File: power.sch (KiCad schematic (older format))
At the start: 19 parts, among them P1 CONN_01X02, P2 CONN_01X02, P3 CONN_01X02, P4 CONN_01X02, U1 MC34063

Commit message: - added wifi esp8266 - switched caps to smd - fixed dual transistor pinout bug
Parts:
- C1, C2: footprint capacitors:C_0805 -> capacitors:C_1206
- U1: symbol MC34063 -> MC34063-RESCUE-rados
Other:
- moved on the sheet: R1, R2, R3
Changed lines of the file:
@@
 EESchema Schematic File Version 2
+LIBS:rados-rescue
+LIBS:import-transistors
+LIBS:import-regulators
+LIBS:import-opamps
+LIBS:import-diodes
 LIBS:led_reverse
 LIBS:arduino_shieldsNCL
 LIBS:otheruse_transistors
 LIBS:custom_power
-LIBS:import_resistors
-LIBS:import_regulators
-LIBS:import_transistors
-LIBS:import_diodes
+LIBS:import-misc
+LIBS:armin_misc
 LIBS:power
 LIBS:device
 LIBS:transistors
 LIBS:conn
-LIBS:import_misc
 LIBS:linear
 LIBS:regul
@@
 LIBS:valves
 LIBS:arduino
+LIBS:ESP8266
 LIBS:rados-cache
 EELAYER 25 0
@@
 	4400 1925 4400 2625
 $Comp
-L MC34063 U1
+L MC34063-RESCUE-rados U1
 U 1 1 568AB185
 P 2025 2100
+AR Path="/568AB185" Ref="U1"  Part="1"
+AR Path="/568AA436/568AB185" Ref="U1"  Part="1"
 F 0 "U1" H 2425 2475 34  0000 C BNN
 F 1 "MC34063" H 2425 2150 34  0000 C BNN
@@
 $EndComp
 Wire Wire Line
-	1525 1925 2075 1925
+	1525 1925 2025 1925
 $Comp
 L STPS3L40UF D1
@@
 L RESISTOR R2
 U 1 1 568AB18A
-P 3725 1825
-F 0 "R2" V 3875 1750 34  0000 L BNN
-F 1 "10K" H 3825 1900 34  0000 L BNN
-F 2 "resistors:R_0603" H 3725 1825 60  0001 C CNN
-F 3 "" H 3725 1825 60  0000 C CNN
-	1    3725 1825
+P 3675 1825
+F 0 "R2" V 3825 1750 34  0000 L BNN
+F 1 "10K" H 3775 1900 34  0000 L BNN
+F 2 "resistors:R_0603" H 3675 1825 60  0001 C CNN
+F 3 "" H 3675 1825 60  0000 C CNN
+	1    3675 1825
 	0    1    1    0
 $EndComp
@@
 L RESISTOR R3
 U 1 1 568AB18B
-P 3725 2100
-F 0 "R3" V 3875 2175 34  0000 L BNN
-F 1 "1K1" H 3800 2050 34  0000 L BNN
-F 2 "resistors:R_0603" H 3725 2100 60  0001 C CNN
-F 3 "" H 3725 2100 60  0000 C CNN
-	1    3725 2100
+P 3675 2100
+F 0 "R3" V 3825 2175 34  0000 L BNN
+F 1 "1K1" H 3750 2050 34  0000 L BNN
+F 2 "resistors:R_0603" H 3675 2100 60  0001 C CNN
+F 3 "" H 3675 2100 60  0000 C CNN
+	1    3675 2100
 	0    1    1    0
 $EndComp
@@
 L RESISTOR R1
 U 1 1 568AB18D
-P 1750 1850
-F 0 "R1" H 1850 1900 34  0000 L BNN
-F 1 "0.22R" H 1800 1800 34  0000 L BNN
-F 2 "resistors:R_1206" H 1750 1850 60  0001 C CNN
-F 3 "" H 1750 1850 60  0000 C CNN
-	1    1750 1850
+P 1750 1900
+F 0 "R1" H 1825 2025 34  0000 L BNN
+F 1 "0.22R" H 1800 1900 34  0000 L BNN
+F 2 "resistors:R_1206" H 1750 1900 60  0001 C CNN
+F 3 "" H 1750 1900 60  0000 C CNN
+	1    1750 1900
 	1    0    0    -1
 $EndComp
@@
 F 0 "C1" H 1535 2145 50  0000 L CNN
 F 1 "10uF" H 1535 1995 50  0000 L CNN
-F 2 "capacitors:C_0805" H 1525 2075 50  0001 C CNN
+F 2 "capacitors:C_1206" H 1525 2075 50  0001 C CNN
 F 3 "" H 1525 2075 50  0000 C CNN
 	1    1525 2075
@@
 F 0 "C2" H 1760 2145 50  0000 L CNN
 F 1 "10uF" H 1760 1995 50  0000 L CNN
-F 2 "capacitors:C_0805" H 1750 2075 50  0001 C CNN
+F 2 "capacitors:C_1206" H 1750 2075 50  0001 C CNN
 F 3 "" H 1750 2075 50  0000 C CNN
 	1    1750 2075
@@
 $EndComp
 $Comp
-L +12V #PWR06
+L +12V #PWR49
 U 1 1 568AC408
 P 5150 1925
-F 0 "#PWR06" H 5150 1775 50  0001 C CNN
+F 0 "#PWR49" H 5150 1775 50  0001 C CNN
 F 1 "+12V" H 5168 2099 50  0000 C CNN
 F 2 "" H 5150 1925 50  0000 C CNN
@@
 $EndComp
 $Comp
-L GND #PWR07
+L GND #PWR4
 U 1 1 568AE875
 P 1425 4450
-F 0 "#PWR07" H 1425 4200 50  0001 C CNN
+F 0 "#PWR4" H 1425 4200 50  0001 C CNN
 F 1 "GND" H 1433 4276 50  0000 C CNN
 F 2 "" H 1425 4450 50  0000 C CNN
@@
 $EndComp
 $Comp
-L GND #PWR08
+L GND #PWR23
 U 1 1 568AE8A5
 P 2800 2325
-F 0 "#PWR08" H 2800 2075 50  0001 C CNN
+F 0 "#PWR23" H 2800 2075 50  0001 C CNN
 F 1 "GND" H 2808 2151 50  0000 C CNN
 F 2 "" H 2800 2325 50  0000 C CNN
@@
 	1500 4350 1425 4350
 $Comp
-L Vsupply #P09
+L Vsupply #P11
 U 1 1 568AD53F
 P 4750 1225
-F 0 "#P09" H 4750 1225 60  0001 C CNN
+F 0 "#P11" H 4750 1225 60  0001 C CNN
 F 1 "Vsupply" H 4750 1175 34  0000 C CNN
 F 2 "" H 4750 1225 60  0000 C CNN
@@
 $EndComp
 $Comp
-L Vsupply #P010
+L Vsupply #P1
 U 1 1 568AD70E
 P 1525 1775
-F 0 "#P010" H 1525 1775 60  0001 C CNN
+F 0 "#P1" H 1525 1775 60  0001 C CNN
 F 1 "Vsupply" H 1525 1725 34  0000 C CNN
 F 2 "" H 1525 1775 60  0000 C CNN
@@
 $EndComp
 $Comp
-L GND #PWR011
+L GND #PWR6
 U 1 1 568ADBA9
 P 1450 3800
-F 0 "#PWR011" H 1450 3550 50  0001 C CNN
+F 0 "#PWR6" H 1450 3550 50  0001 C CNN
 F 1 "GND" H 1458 3626 50  0000 C CNN
 F 2 "" H 1450 3800 50  0000 C CNN
@@
 	1525 3700 1450 3700
 $Comp
-L Vsupply #P012
+L Vsupply #P4
 U 1 1 568ADC9C
 P 2125 3550
-F 0 "#P012" H 2125 3550 60  0001 C CNN
+F 0 "#P4" H 2125 3550 60  0001 C CNN
 F 1 "Vsupply" H 2125 3500 34  0000 C CNN
 F 2 "" H 2125 3550 60  0000 C CNN
@@
 $EndComp
 $Comp
-L Vheatbed #P013
+L Vheatbed #P3
 U 1 1 568AE31D
 P 2100 4200
-F 0 "#P013" H 2100 4200 60  0001 C CNN
+F 0 "#P3" H 2100 4200 60  0001 C CNN
 F 1 "Vheatbed" H 2100 4150 34  0000 C CNN
 F 2 "" H 2100 4200 60  0000 C CNN
@@
 $EndComp
 $Comp
-L GND #PWR014
+L GND #PWR9
 U 1 1 568AE68D
 P 1475 5400
-F 0 "#PWR014" H 1475 5150 50  0001 C CNN
+F 0 "#PWR9" H 1475 5150 50  0001 C CNN
 F 1 "GND" H 1483 5226 50  0000 C CNN
 F 2 "" H 1475 5400 50  0000 C CNN
@@
 	1475 5300 1650 5300
 $Comp
-L Vsupply #P015
+L Vsupply #P2
 U 1 1 568AE69B
 P 1650 5150
-F 0 "#P015" H 1650 5150 60  0001 C CNN
+F 0 "#P2" H 1650 5150 60  0001 C CNN
 F 1 "Vsupply" H 1650 5100 34  0000 C CNN
 F 2 "" H 1650 5150 60  0000 C CNN
@@
 $EndComp
 $Comp
-L GND #PWR016
+L GND #PWR10
 U 1 1 568AE860
 P 1475 6475
-F 0 "#PWR016" H 1475 6225 50  0001 C CNN
+F 0 "#PWR10" H 1475 6225 50  0001 C CNN
 F 1 "GND" H 1483 6301 50  0000 C CNN
 F 2 "" H 1475 6475 50  0000 C CNN
@@
 	1475 6375 1650 6375
 $Comp
-L +12V #PWR017
+L +12V #PWR11
 U 1 1 568BD457
 P 1650 6375
-F 0 "#PWR017" H 1650 6225 50  0001 C CNN
+F 0 "#PWR11" H 1650 6225 50  0001 C CNN
 F 1 "+12V" H 1668 6549 50  0000 C CNN
 F 2 "" H 1650 6375 50  0000 C CNN

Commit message: Routing
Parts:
- added P23, P24: CONN_01X02, headers:CON_HDR_1x2_2.54mm, symbol CONN_01X02
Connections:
- net +12V: now also P24.2 (P2)
- net GND: now also P23.1 (P1), P24.1 (P1)
- net Vsupply: now also P23.2 (P2)
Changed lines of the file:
@@
 $EndComp
 $Comp
-L +12V #PWR49
+L +12V #PWR15
 U 1 1 568AC408
 P 5150 1925
-F 0 "#PWR49" H 5150 1775 50  0001 C CNN
+F 0 "#PWR15" H 5150 1775 50  0001 C CNN
 F 1 "+12V" H 5168 2099 50  0000 C CNN
 F 2 "" H 5150 1925 50  0000 C CNN
@@
 $EndComp
 $Comp
-L GND #PWR4
+L GND #PWR6
 U 1 1 568AE875
 P 1425 4450
-F 0 "#PWR4" H 1425 4200 50  0001 C CNN
+F 0 "#PWR6" H 1425 4200 50  0001 C CNN
 F 1 "GND" H 1433 4276 50  0000 C CNN
 F 2 "" H 1425 4450 50  0000 C CNN
@@
 $EndComp
 $Comp
-L GND #PWR23
+L GND #PWR14
 U 1 1 568AE8A5
 P 2800 2325
-F 0 "#PWR23" H 2800 2075 50  0001 C CNN
+F 0 "#PWR14" H 2800 2075 50  0001 C CNN
 F 1 "GND" H 2808 2151 50  0000 C CNN
 F 2 "" H 2800 2325 50  0000 C CNN
@@
 	1500 4350 1425 4350
 $Comp
-L Vsupply #P11
+L Vsupply #P6
 U 1 1 568AD53F
 P 4750 1225
-F 0 "#P11" H 4750 1225 60  0001 C CNN
+F 0 "#P6" H 4750 1225 60  0001 C CNN
 F 1 "Vsupply" H 4750 1175 34  0000 C CNN
 F 2 "" H 4750 1225 60  0000 C CNN
@@
 $EndComp
 $Comp
-L GND #PWR6
+L GND #PWR7
 U 1 1 568ADBA9
 P 1450 3800
-F 0 "#PWR6" H 1450 3550 50  0001 C CNN
+F 0 "#PWR7" H 1450 3550 50  0001 C CNN
 F 1 "GND" H 1458 3626 50  0000 C CNN
 F 2 "" H 1450 3800 50  0000 C CNN
@@
 	1525 3700 1450 3700
 $Comp
-L Vsupply #P4
+L Vsupply #P5
 U 1 1 568ADC9C
 P 2125 3550
-F 0 "#P4" H 2125 3550 60  0001 C CNN
+F 0 "#P5" H 2125 3550 60  0001 C CNN
 F 1 "Vsupply" H 2125 3500 34  0000 C CNN
 F 2 "" H 2125 3550 60  0000 C CNN
@@
 $EndComp
 $Comp
-L Vheatbed #P3
+L Vheatbed #P4
 U 1 1 568AE31D
 P 2100 4200
-F 0 "#P3" H 2100 4200 60  0001 C CNN
+F 0 "#P4" H 2100 4200 60  0001 C CNN
 F 1 "Vheatbed" H 2100 4150 34  0000 C CNN
 F 2 "" H 2100 4200 60  0000 C CNN
@@
 	1    0    0    -1
 $EndComp
+Connection ~ 2025 1725
+$Comp
+L GND #PWR8
+U 1 1 56BC5BCA
+P 1625 5325
+F 0 "#PWR8" H 1625 5075 50  0001 C CNN
+F 1 "GND" H 1633 5151 50  0000 C CNN
+F 2 "" H 1625 5325 50  0000 C CNN
+F 3 "" H 1625 5325 50  0000 C CNN
+	1    1625 5325
+	1    0    0    -1
+$EndComp
+Wire Wire Line
+	1550 5175 1625 5175
+Wire Wire Line
+	1550 5275 1625 5275
+Wire Wire Line
+	1625 5275 1625 5325
+$Comp
+L Vsupply #P2
+U 1 1 56BC5C4C
+P 1625 5025
+F 0 "#P2" H 1625 5025 60  0001 C CNN
+F 1 "Vsupply" H 1625 4975 34  0000 C CNN
+F 2 "" H 1625 5025 60  0000 C CNN
+F 3 "" H 1625 5025 60  0000 C CNN
+	1    1625 5025
+	1    0    0    -1
+$EndComp
 $Comp
 L CONN_01X02 P3
-U 1 1 568AE687
-P 1275 5350
-F 0 "P3" H 1275 5175 50  0000 C CNN
-F 1 "CONN_01X02" H 1194 5160 50  0001 C CNN
-F 2 "headers:CON_HDR_1x2_2.54mm" H 1275 5350 50  0001 C CNN
-F 3 "" H 1275 5350 50  0000 C CNN
-	1    1275 5350
-	-1   0    0    1
+U 1 1 56BC61F9
+P 1350 5225
+F 0 "P3" H 1350 5050 50  0000 C CNN
+F 1 "CONN_01X02" H 1675 5225 50  0000 C CNN
+F 2 "headers:CON_HDR_1x2_2.54mm" H 1350 5225 50  0001 C CNN
+F 3 "" H 1350 5225 50  0000 C CNN
+	1    1350 5225
+	-1   0    0    1
+$EndComp
+$Comp
+L GND #PWR11
+U 1 1 56BC656B
+P 1625 6475
+F 0 "#PWR11" H 1625 6225 50  0001 C CNN
+F 1 "GND" H 1633 6301 50  0000 C CNN
+F 2 "" H 1625 6475 50  0000 C CNN
+F 3 "" H 1625 6475 50  0000 C CNN
+	1    1625 6475
+	1    0    0    -1
+$EndComp
+Wire Wire Line
+	1550 6325 1625 6325
+Wire Wire Line
+	1550 6425 1625 6425
+Wire Wire Line
+	1625 6425 1625 6475
+$Comp
+L CONN_01X02 P4
+U 1 1 56BC657A
+P 1350 6375
+F 0 "P4" H 1350 6200 50  0000 C CNN
+F 1 "CONN_01X02" H 1675 6375 50  0000 C CNN
+F 2 "headers:CON_HDR_1x2_2.54mm" H 1350 6375 50  0001 C CNN
+F 3 "" H 1350 6375 50  0000 C CNN
+	1    1350 6375
+	-1   0    0    1
+$EndComp
+$Comp
+L +12V #PWR10
+U 1 1 56BC66FC
+P 1625 6325
+F 0 "#PWR10" H 1625 6175 50  0001 C CNN
+F 1 "+12V" H 1643 6499 50  0000 C CNN
+F 2 "" H 1625 6325 50  0000 C CNN
+F 3 "" H 1625 6325 50  0000 C CNN
+	1    1625 6325
+	1    0    0    -1
 $EndComp
 $Comp
 L GND #PWR9
-U 1 1 568AE68D
-P 1475 5400
-F 0 "#PWR9" H 1475 5150 50  0001 C CNN
-F 1 "GND" H 1483 5226 50  0000 C CNN
-F 2 "" H 1475 5400 50  0000 C CNN
-F 3 "" H 1475 5400 50  0000 C CNN
-	1    1475 5400
-	1    0    0    -1
-$EndComp
-Wire Wire Line
-	1475 5300 1650 5300
-$Comp
-L Vsupply #P2
-U 1 1 568AE69B
-P 1650 5150
-F 0 "#P2" H 1650 5150 60  0001 C CNN
-F 1 "Vsupply" H 1650 5100 34  0000 C CNN
-F 2 "" H 1650 5150 60  0000 C CNN
-F 3 "" H 1650 5150 60  0000 C CNN
-	1    1650 5150
-	1    0    0    -1
-$EndComp
-$Comp
-L CONN_01X02 P4
-U 1 1 568AE85A
-P 1275 6425
-F 0 "P4" H 1275 6250 50  0000 C CNN
-F 1 "CONN_01X02" H 1194 6235 50  0001 C CNN
-F 2 "headers:CON_HDR_1x2_2.54mm" H 1275 6425 50  0001 C CNN
-F 3 "" H 1275 6425 50  0000 C CNN
-	1    1275 6425
-	-1   0    0    1
-$EndComp
-$Comp
-L GND #PWR10
-U 1 1 568AE860
-P 1475 6475
-F 0 "#PWR10" H 1475 6225 50  0001 C CNN
-F 1 "GND" H 1483 6301 50  0000 C CNN
-F 2 "" H 1475 6475 50  0000 C CNN
-F 3 "" H 1475 6475 50  0000 C CNN
-	1    1475 6475
-	1    0    0    -1
-$EndComp
-Wire Wire Line
-	1475 6375 1650 6375
-$Comp
-L +12V #PWR11
-U 1 1 568BD457
-P 1650 6375
-F 0 "#PWR11" H 1650 6225 50  0001 C CNN
-F 1 "+12V" H 1668 6549 50  0000 C CNN
-F 2 "" H 1650 6375 50  0000 C CNN
-F 3 "" H 1650 6375 50  0000 C CNN
-	1    1650 6375
-	1    0    0    -1
-$EndComp
-Connection ~ 2025 1725
+U 1 1 56BC6A92
+P 1625 5850
+F 0 "#PWR9" H 1625 5600 50  0001 C CNN
+F 1 "GND" H 1633 5676 50  0000 C CNN
+F 2 "" H 1625 5850 50  0000 C CNN
+F 3 "" H 1625 5850 50  0000 C CNN
+	1    1625 5850
+	1    0    0    -1
+$EndComp
+Wire Wire Line
+	1550 5700 1625 5700
+Wire Wire Line
+	1550 5800 1625 5800
+Wire Wire Line
+	1625 5800 1625 5850
+$Comp
+L Vsupply #P3
+U 1 1 56BC6A9B
+P 1625 5550
+F 0 "#P3" H 1625 5550 60  0001 C CNN
+F 1 "Vsupply" H 1625 5500 34  0000 C CNN
+F 2 "" H 1625 5550 60  0000 C CNN
+F 3 "" H 1625 5550 60  0000 C CNN
+	1    1625 5550
+	1    0    0    -1
+$EndComp
+$Comp
+L CONN_01X02 P23
+U 1 1 56BC6AA1
+P 1350 5750
+F 0 "P23" H 1350 5575 50  0000 C CNN
+F 1 "CONN_01X02" H 1675 5750 50  0000 C CNN
+F 2 "headers:CON_HDR_1x2_2.54mm" H 1350 5750 50  0001 C CNN
+F 3 "" H 1350 5750 50  0000 C CNN
+	1    1350 5750
+	-1   0    0    1
+$EndComp
+$Comp
+L GND #PWR13
+U 1 1 56BC6B73
+P 1625 7100
+F 0 "#PWR13" H 1625 6850 50  0001 C CNN
+F 1 "GND" H 1633 6926 50  0000 C CNN
+F 2 "" H 1625 7100 50  0000 C CNN
+F 3 "" H 1625 7100 50  0000 C CNN
+	1    1625 7100
+	1    0    0    -1
+$EndComp
+Wire Wire Line
+	1550 6950 1625 6950
+Wire Wire Line
+	1550 7050 1625 7050
+Wire Wire Line
+	1625 7050 1625 7100
+$Comp
+L CONN_01X02 P24
+U 1 1 56BC6B7C
+P 1350 7000
+F 0 "P24" H 1350 6825 50  0000 C CNN
+F 1 "CONN_01X02" H 1675 7000 50  0000 C CNN
+F 2 "headers:CON_HDR_1x2_2.54mm" H 1350 7000 50  0001 C CNN
+F 3 "" H 1350 7000 50  0000 C CNN
+	1    1350 7000
+	-1   0    0    1
+$EndComp
+$Comp
+L +12V #PWR12
+U 1 1 56BC6B82
+P 1625 6950
+F 0 "#PWR12" H 1625 6800 50  0001 C CNN
+F 1 "+12V" H 1643 7124 50  0000 C CNN
+F 2 "" H 1625 6950 50  0000 C CNN
+F 3 "" H 1625 6950 50  0000 C CNN
+	1    1625 6950
+	1    0    0    -1
+$EndComp
 $EndSCHEMATC

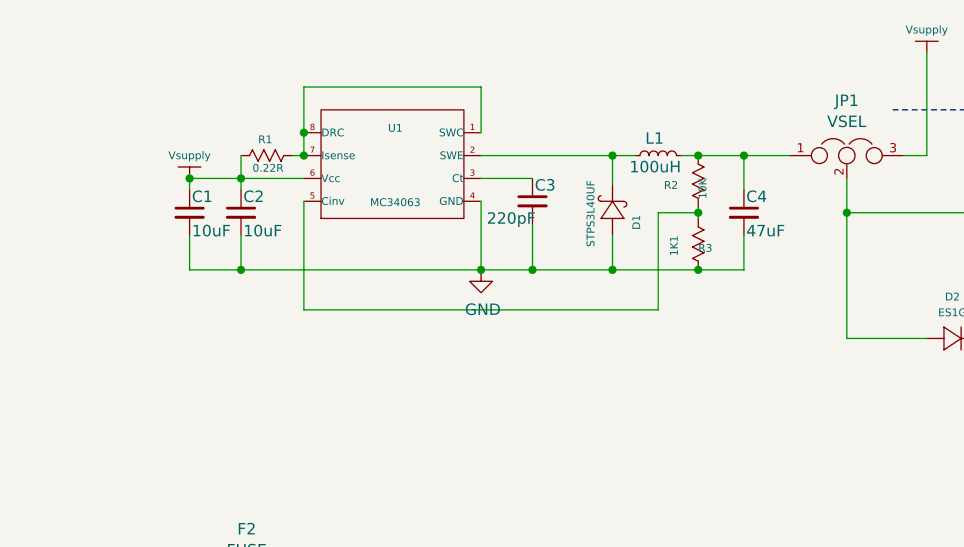
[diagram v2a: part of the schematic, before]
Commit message: Replaced SMPS with ST ic
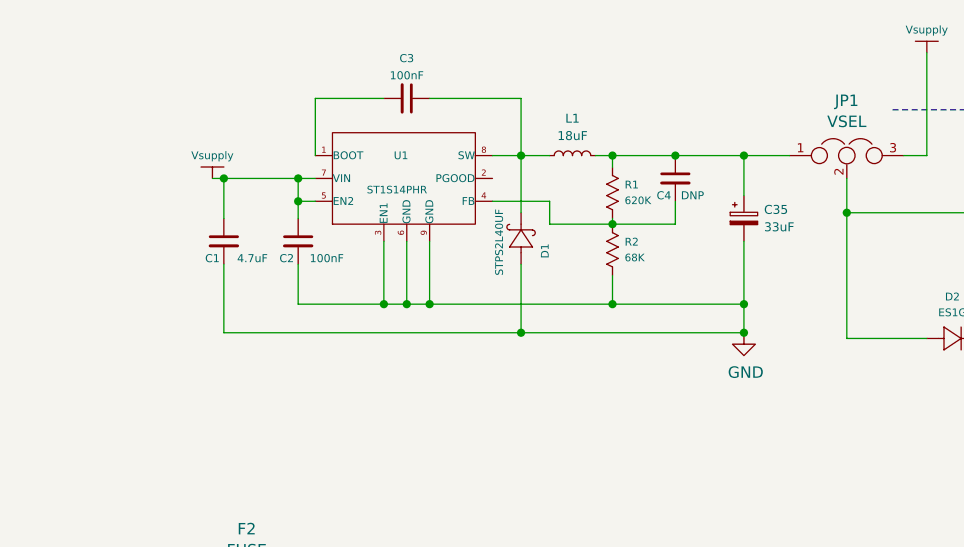
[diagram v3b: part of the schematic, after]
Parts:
- removed R3: 1K1, resistors:R_0603, symbol RESISTOR
- removed U1: MC34063, soic:SOIC8, symbol MC34063-RESCUE-rados
- added C35: 33uF, capacitors:c_elec_6.3x7.7, symbol CP_Small
- added U1: ST1S14PHR, soic:HSOP8, symbol st1s14phr
- C1: value 10uF -> 4.7uF; footprint capacitors:C_1206 -> capacitors:C_1210
- C2: value 10uF -> 100nF; footprint capacitors:C_1206 -> capacitors:C_0603
- C3: value 220pF -> 100nF
- C4: value 47uF -> DNP; footprint capacitors:C_1210 -> capacitors:C_0603; Manufacturer Murata -> (none); ManufacturerNo GRM32EC81C476ME15L -> (none); VoltageRating 16V -> (none)
- D1: value STPS3L40UF -> STPS2L40UF
- L1: value 100uH -> 18uF; footprint inductors:INDUCTOR_AIUR06 -> inductors:INDUCTOR_BOURNS_RLB914
- R1: value 0.22R -> 620K; footprint resistors:R_1206 -> resistors:R_0603
- R2: value 10K -> 68K
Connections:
- net GND: now also R2.2, C35.2, U1.3 (EN1), U1.6 (GND), U1.9 (GND); no longer C3.2, C4.2
- net Vsupply: now also U1.5 (EN2), U1.7 (VIN); no longer R1.1
- net at R1.2: now also C4.2, R2.1, U1.4 (FB)
- net at D1.1 (cathode), L1.1: now also C3.1, U1.8 (SW)
- net at C4.1, JP1.1, L1.2: now also R1.1, C35.1; no longer R2.1
- new net: C3.2, U1.1 (BOOT)
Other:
- moved on the sheet: D1
